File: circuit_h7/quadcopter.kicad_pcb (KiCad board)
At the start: 4 copper layers, 37.5 x 37.5 mm, 128 parts, among them J1 Conn_01x01_Female, J10 Conn_01x01_Female, J11 Conn_01x04_Male, J13 Conn_01x01_Female, J14 Conn_01x01_Female, J15 Conn_01x01_Female, J16 Conn_01x01_Female, J17 Conn_01x01_Female, J18 USB_C_Receptacle_USB2.0, J19 Conn_01x08_Male, J2 Conn_01x01_Female, J20 Conn_01x01_Female, J21 Conn_01x01_Female, J22 Conn_01x01_Female, J23 Conn_01x01_Female, J24 Conn_01x01_Female, J25 Conn_01x01_Female, J26 Conn_01x01_Female, J27 Conn_01x01_Female, J28 Conn_01x01_Female, J29 Conn_01x01_Female, J3 Conn_01x01_Female, J30 Conn_01x01_Female, J31 Conn_01x01_Female, J32 Conn_01x01_Female, J33 Conn_01x01_Female, J34 Conn_01x01_Female, J35 Conn_01x01_Female, J36 Conn_01x01_Female, J37 Conn_01x01_Female, J4 Conn_01x01_Female, J40 Conn_01x01_Female, J41 Conn_01x01_Female, J42 Conn_01x01_Female, J43 Conn_01x01_Female, J44 Conn_01x01_Female, J45 Conn_01x01_Female, J47 Conn_01x01_Female, J48 Conn_01x01_Female, J49 Conn_01x01_Female, J5 Conn_Coaxial, J50 Conn_01x01_Female, J6 Conn_01x06_Male, J7 Conn_01x01_Female, J8 Conn_01x01_Female, J9 Conn_01x01_Female, SW1 SW_DIP_x01, U1 STM32H723VGH6, U10 ESP8285, U12 TPS5430DDA, U2 ICM-42605, U3 DPS310, U4 3V3, U6 2450FM07D0034T, U7 W25Q80DVUXIE TR (16M), U8 SX1281, Y1 16M, Y2 52Mhz, 12pF, Y3 40M

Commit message: More work on fusion
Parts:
- removed C42: 150p, Capacitor_SMD:C_0402_1005Metric
- removed C43: 100n, Capacitor_SMD:C_0402_1005Metric
- removed C44: 1.5n, Capacitor_SMD:C_0402_1005Metric
- removed C45, C46: 10u, Capacitor_SMD:C_0805_2012Metric
- removed R17: 300, Resistor_SMD:R_0402_1005Metric
- removed R19: 10k, Resistor_SMD:R_0402_1005Metric
- added C14: 22uF 25v, Capacitor_SMD:C_0805_2012Metric, F.Cu at (132.2, 99.5)
- added C15: 22n, Capacitor_SMD:C_0402_1005Metric, F.Cu at (128.0, 97.2)
- added C20: 100uF 6.3V, Capacitor_SMD:C_1206_3216Metric, F.Cu at (136.0, 94.0)
- added J38: Conn_01x01_Female, TestPoint:TestPoint_Pad_1.0x1.0mm, B.Cu at (147.5, 77.5)
- added L2: 10u 2A, Inductor_SMD:L_Taiyo-Yuden_MD-4040, F.Cu at (131.2, 95.5)
- added R7: 10k, Resistor_SMD:R_0402_1005Metric, F.Cu at (150.5, 97.8)
- added R8: 100k, Resistor_SMD:R_0402_1005Metric, F.Cu at (124.8, 99.5)
- added U5: MT2492 600kHz 16v 2A, Package_TO_SOT_SMD:SOT-23-6, F.Cu at (129.0, 99.5)
- R10: value 3.3K -> 1.4k
- R11: value 300 -> 13k; footprint Resistor_SMD:R_0402_1005Metric -> Resistor_SMD:R_0603_1608Metric
- U12: value TPS5430DDA -> TPS5430DDA 3A 36v
- moved J35 40.7 mm to (144.0, 79.0)
- moved J36 39.4 mm to (146.0, 81.0)
- moved J34 38.4 mm to (144.0, 81.0)
- moved J27 31.3 mm to (146.0, 79.0)
- moved R11 23.9 mm to (126.0, 99.8)
- moved F1 12.4 mm to (115.2, 94.0), turned to 180 degrees
- moved R10 1.06 mm to (150.5, 98.8)
- moved D1 0.50 mm to (126.0, 104.2)
- moved C40 0.25 mm to (132.2, 103.8)
- moved C41 0.25 mm to (128.8, 103.8)
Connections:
- net Net-(R9-Pad2) renamed /ELRS_LED
- D5 pad 2: unconnected-(D5-Pad2) -> Net-(C20-Pad1)
- R10 pad 2: Net-(C43-Pad2) -> Net-(R10-Pad2)
- R11 pad 2: Net-(C42-Pad1) -> Net-(R8-Pad1)
- U10 pad 15: unconnected-(U10-Pad15) -> /ELRS_BOOT
- U12 pad 4: Net-(C42-Pad1) -> Net-(R10-Pad2)
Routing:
- net Net-(C20-Pad1): track 0.00 -> 15.9 mm, vias 0 -> 2
- net /ELRS_LED: track 11.3 -> 24.0 mm, vias 2 -> 3
- net /UART1_RX: track 55.6 -> 44.4 mm, vias 6 -> 4
- net Net-(C42-Pad1): track 10.8 -> 0.00 mm
- net Net-(R10-Pad2): track 0.00 -> 8.21 mm
- net /IMU_pwr: track 26.0 -> 19.1 mm
- net /USB_DP: track 24.0 -> 18.7 mm
- net Net-(L2-Pad1): track 0.00 -> 4.96 mm
- net +10V: track 63.1 -> 58.3 mm
- net /USB_DN: track 23.8 -> 19.6 mm
- net Net-(R8-Pad1): track 0.00 -> 3.46 mm
- net GND: track 47.6 -> 49.7 mm
- net /BATT_DIV: track 11.4 -> 9.43 mm
- net Net-(D1-Pad2): track 1.51 -> 0.00 mm
- net Net-(C15-Pad1): track 0.00 -> 1.44 mm
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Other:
- board text added: "B"
- board text added: "C"
- board text added: "D"
- board text added: "R"
- board text added: "T"

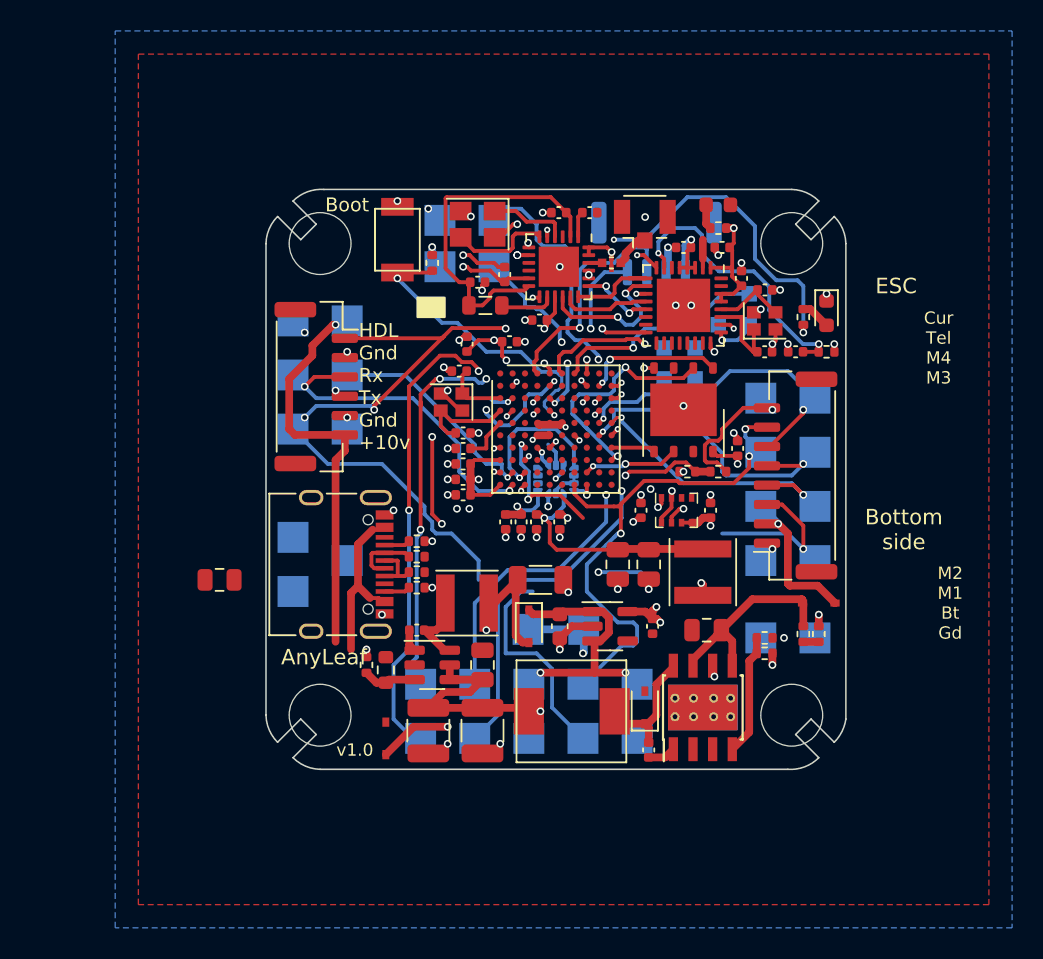
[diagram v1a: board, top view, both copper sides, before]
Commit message: Added timer ARR/PSC and clock config speeds for H743@480Mhz, H723 at 520 and 550Mhz
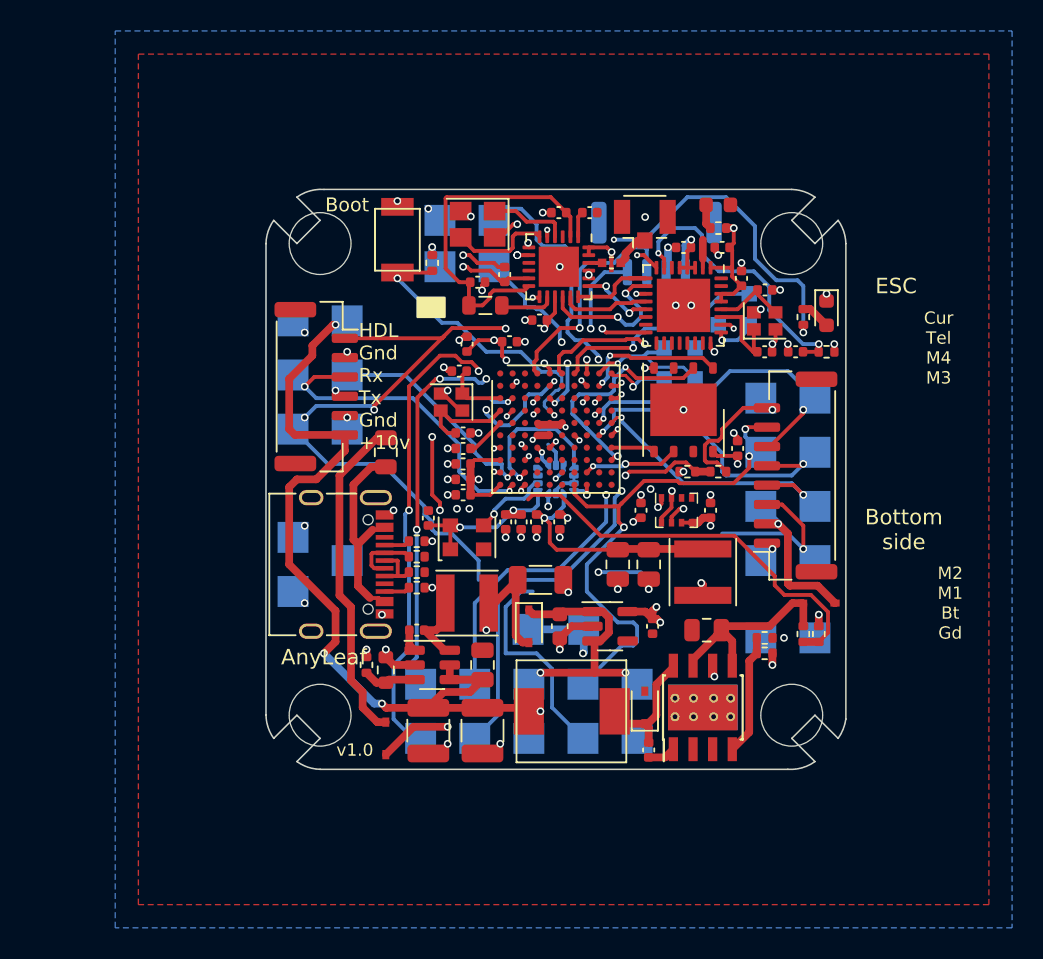
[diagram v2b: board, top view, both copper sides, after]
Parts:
- added C21: 100n, Capacitor_SMD:C_0402_1005Metric, F.Cu at (128.8, 90.0)
- added X1: TXC-7C, Oscillator:Oscillator_SMD_EuroQuartz_XO32-4Pin_3.2x2.5mm, F.Cu at (131.2, 91.2)
- moved F1 13.6 mm to (126.0, 85.8), turned to -90 degrees
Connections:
- net /IMU_pwr renamed /IMU_PWR
- C15 pad 2: Net-(L2-Pad1) -> Net-(C15-Pad2)
- L2 pad 1: Net-(L2-Pad1) -> Net-(C15-Pad2)
- R11 pad 2: Net-(R8-Pad1) -> Net-(R11-Pad2)
- R8 pad 1: Net-(R8-Pad1) -> Net-(R11-Pad2)
- U2 pad 9: unconnected-(U2-Pad9) -> Net-(U2-Pad9)
- U5 pad 1: +10V -> Net-(C15-Pad1)
- U5 pad 2: unconnected-(U5-Pad2) -> GND
- U5 pad 3: +10V -> Net-(R11-Pad2)
- U5 pad 4: Net-(R8-Pad1) -> +10V
- U5 pad 5: Net-(C15-Pad1) -> +10V
- U5 pad 6: unconnected-(U5-Pad6) -> Net-(C15-Pad2)
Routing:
- net Net-(D1-Pad2): track 0.00 -> 21.5 mm
- net /BATT_DIV: track 9.43 -> 26.5 mm, vias 2 -> 1
- net +5V: track 27.9 -> 41.5 mm, vias 3 -> 4
- net +10V: track 58.3 -> 70.8 mm, vias 3 -> 5
- net /IMU_PWR: track 19.1 -> 26.6 mm, vias 2 -> 3
- net Net-(U2-Pad9): track 0.00 -> 5.01 mm, vias 0 -> 1
- net Net-(L2-Pad1): track 4.96 -> 0.00 mm
- net Net-(C15-Pad2): track 0.00 -> 4.96 mm
- net /SWCLK: track 0.00 -> 4.88 mm, vias 0 -> 1
- net /SWDIO: track 0.00 -> 4.12 mm, vias 0 -> 1
- net Net-(R8-Pad1): track 3.46 -> 0.00 mm
- net Net-(R11-Pad2): track 0.00 -> 3.46 mm
- net /NRST: track 3.04 -> 6.27 mm
- net GND: track 49.7 -> 52.2 mm, vias 66 -> 68
- net Net-(F1-Pad2): track 11.3 -> 13.6 mm
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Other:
- outline, holes or cut-outs redrawn

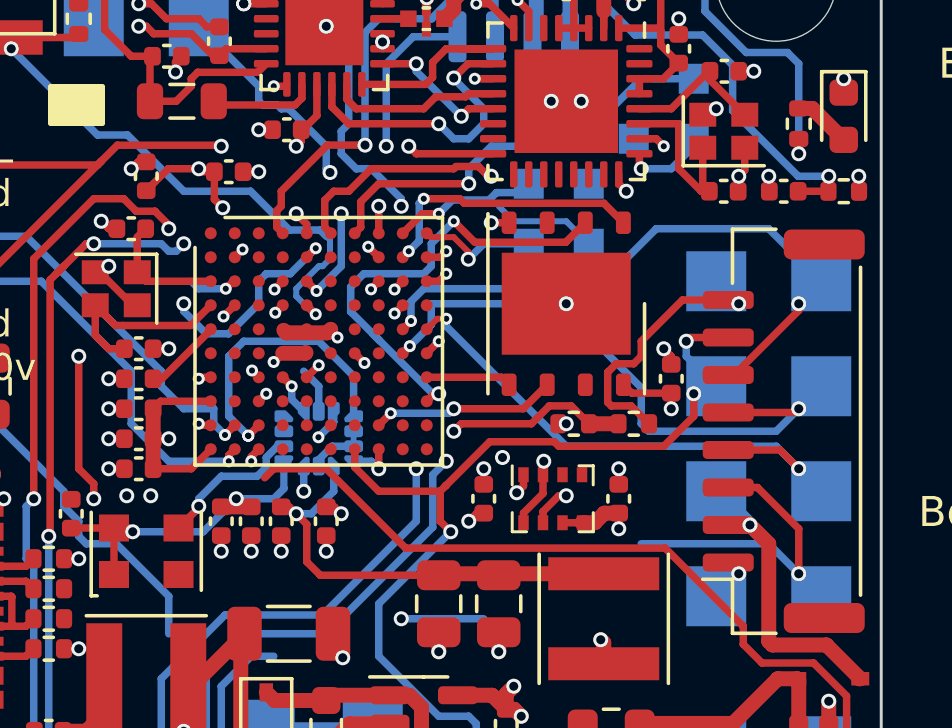
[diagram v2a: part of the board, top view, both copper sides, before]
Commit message: G4 model: Removed 10v line and prev 5v reg
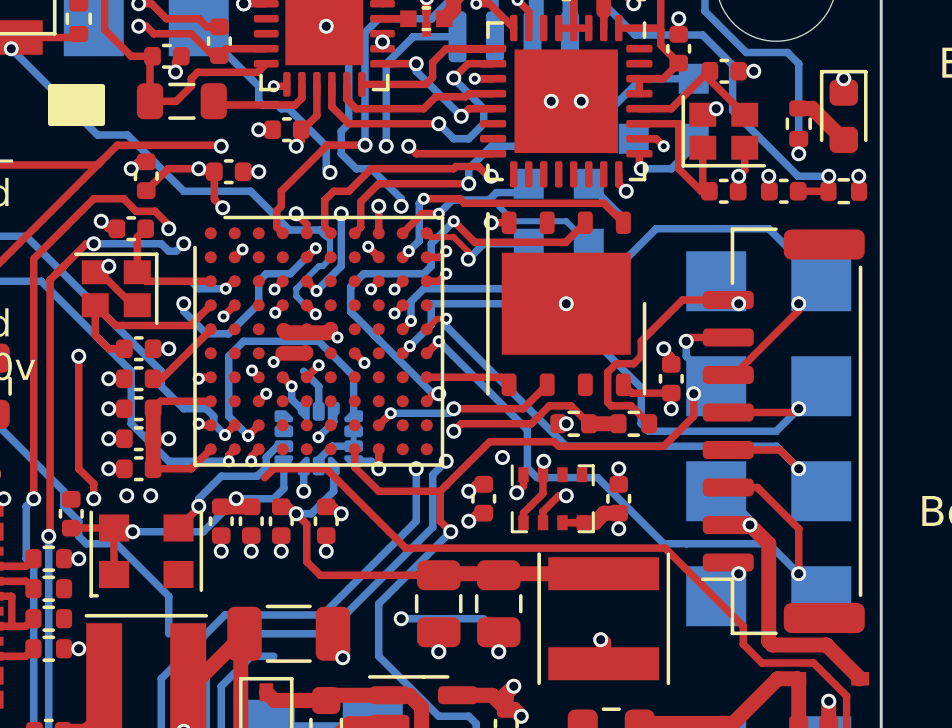
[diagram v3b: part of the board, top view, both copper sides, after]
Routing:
- net /M1: track 10.6 -> 20.9 mm
- net GND: track 52.2 -> 54.5 mm, vias 68 -> 69
- net /SDA2: track 28.1 -> 27.6 mm, vias 3 -> 2
